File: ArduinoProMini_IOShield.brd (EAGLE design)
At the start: 68.6 x 53.3 mm, 29 parts, among them J0 POWER_JACKSLT, J1 Analog, J14 AVR_SPI_PROG_3X2PTH, J2 VCC-Analog, J3 GND-Analog, J4 Digital 0-7, J5 VCC_Digital, J6 GND-Digital, J7 Digital 8-13, J8 VCC-Digital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

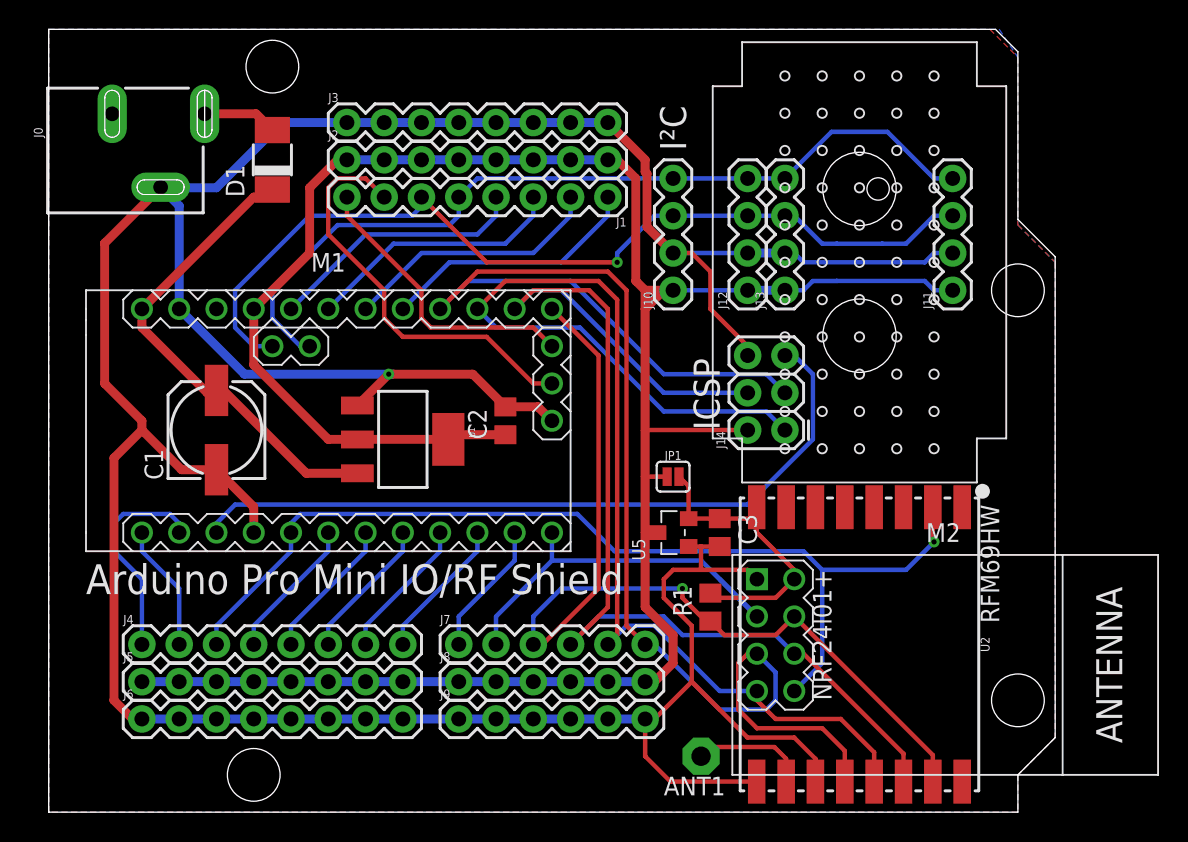
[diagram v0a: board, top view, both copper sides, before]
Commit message: V0.2: Add power soldering connection, add altenative ProMini pinout, move ICSP header; Add pictures;
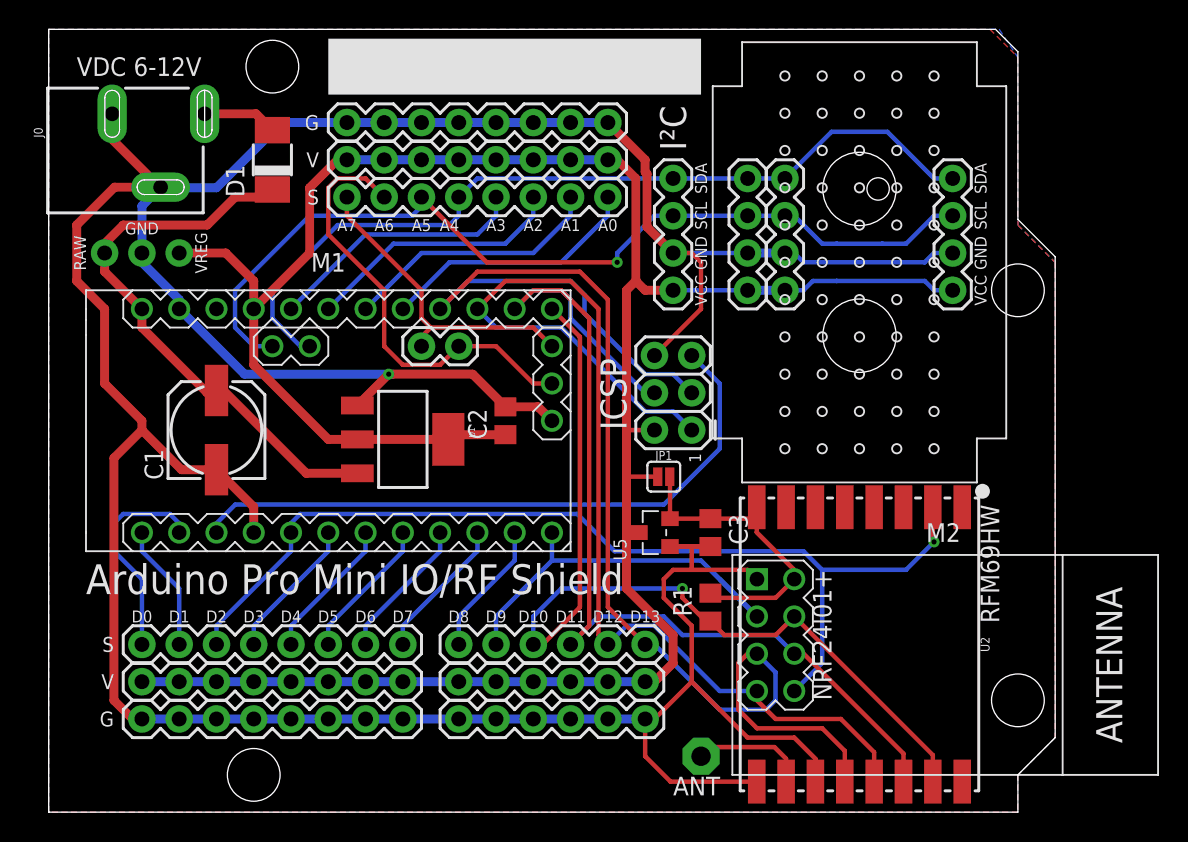
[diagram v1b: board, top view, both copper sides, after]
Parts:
- added J15: orig.conn., SparkFun-Connectors:1X02
- added J16: (no value), SparkFun-Connectors:1X03_NO_SILK
- C1, C2: value (none) -> 10-100µF
- moved J14 6.35 mm to (43.8, 26.0)
- moved U5 1.27 mm to (41.3, 19.1)
- moved JP1 0.64 mm to (41.9, 22.9)
- moved C3 0.63 mm to (45.1, 19.1)
- renumbered ANT1 to ANT
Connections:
- net A6: now also J15.1
- net A7: now also J15.2
- net GND: now also J0.GND@1, J16.2
- net RAW: now also J16.1
- net VCC: now also J16.3
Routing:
- net GND: track 245.7 -> 260.0 mm
- net D12: track 83.6 -> 75.6 mm
- net D11: track 79.9 -> 72.1 mm
- net D13: track 96.3 -> 89.6 mm
- net RST: track 50.5 -> 44.2 mm
- net RAW: track 32.5 -> 38.7 mm
- net VCC: track 161.2 -> 165.3 mm
- net A6: track 28.3 -> 30.5 mm
- net A7: track 20.0 -> 21.6 mm
- net D10: track 64.2 -> 63.2 mm
- net VCC_3.3V: track 20.8 -> 21.8 mm
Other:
- board text added: "1"
- board text added: "Brd:"
- board text added: "Design by R. Kainhofer Version 0.2, December 12, 2017 Licensed under the CERN OHL v1.2"
- board text added: "RAW"
- board text added: "VDC 6-12V"
- board text added: "VREG"
- board text removed: "Design by R. Kainhofer Version 0.1, December 5, 2017 Licensed under teh CERN OHL v1.2"
- board text removed: "VCC 6-40V"
